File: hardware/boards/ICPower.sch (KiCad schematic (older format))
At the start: 2 parts

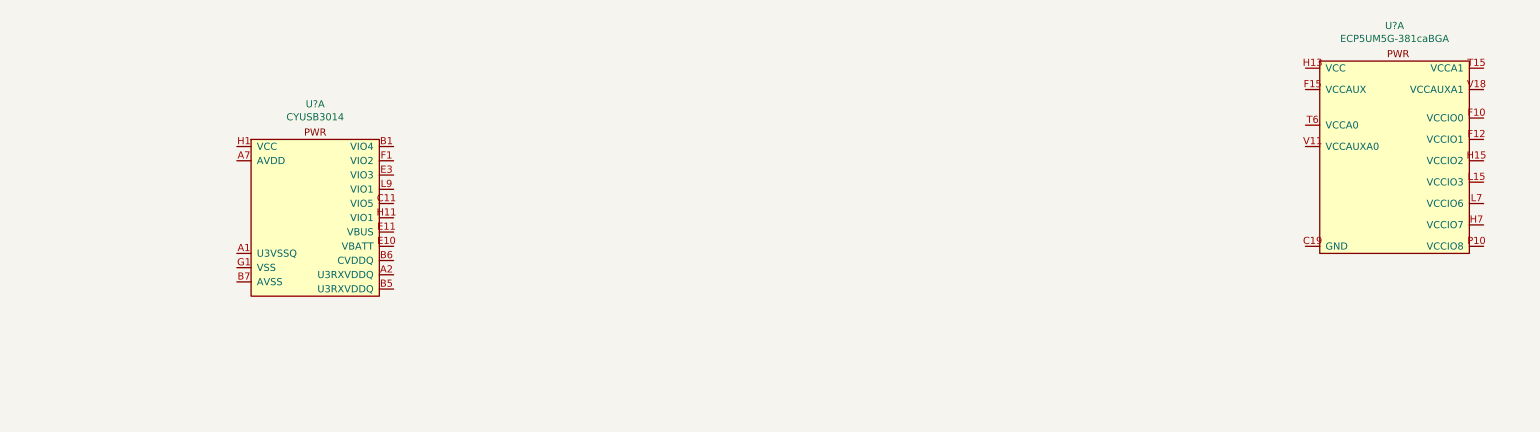
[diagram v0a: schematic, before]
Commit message: Updated part mfr and added the proper part numbers
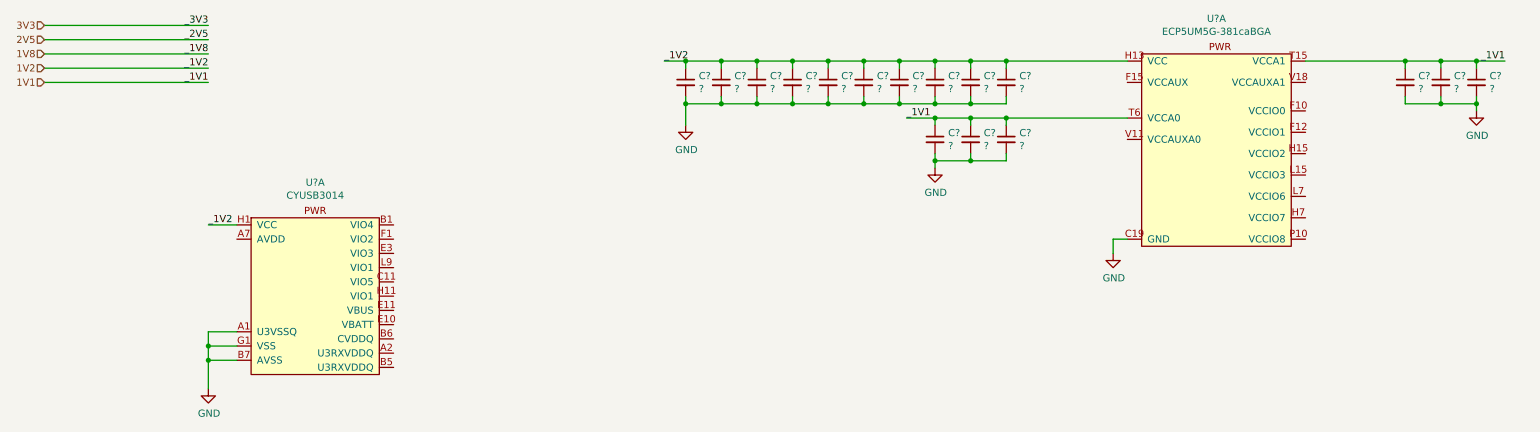
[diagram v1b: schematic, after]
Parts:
- added C? (x16): ?, symbol Device:C_Small
- U?: MFR (none) -> Lattice; MPN (none) -> LFE5UM5G-85F-8BG381I
- U?: MFR (none) -> Cypress; MPN (none) -> CYUSB3014-BZXI
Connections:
- net GND: now reaches U?.B14 (GND), U?.B7 (GND), U?.C19 (GND), U?.D4 (GND), U?.F13 (GND), U?.F14 (GND), U?.F7 (GND), U?.F8 (GND), U?.G10 (GND), U?.G11 (GND), U?.G12 (GND), U?.G13 (GND), U?.G14 (GND), U?.G15 (GND), U?.G17 (GND), U?.G4 (GND), U?.G6 (GND), U?.G7 (GND), U?.G8 (GND), U?.G9 (GND), U?.H19 (GND), U?.J10 (GND), U?.J11 (GND), U?.J12 (GND), U?.J14 (GND), U?.J2 (GND), U?.J7 (GND), U?.J9 (GND), U?.K10 (GND), U?.K11 (GND), U?.K12 (GND), U?.K14 (GND), U?.K15 (GND), U?.K6 (GND), U?.K7 (GND), U?.K9 (GND), U?.L10 (GND), U?.L11 (GND), U?.L12 (GND), U?.L9 (GND), U?.M10 (GND), U?.M11 (GND), U?.M12 (GND), U?.M14 (GND), U?.M16 (GND), U?.M2 (GND), U?.M7 (GND), U?.M9 (GND), U?.N14 (GND), U?.N15 (GND), U?.N6 (GND), U?.N7 (GND), U?.P11 (GND), U?.P12 (GND), U?.P13 (GND), U?.P14 (GND), U?.P7 (GND), U?.P8 (GND), U?.R19 (GND), U?.U10 (GND), U?.U11 (GND), U?.U12 (GND), U?.U13 (GND), U?.U14 (GND), U?.U7 (GND), U?.U8 (GND), U?.U9 (GND), U?.V12 (GND), U?.V13 (GND), U?.V14 (GND), U?.V15 (GND), U?.V16 (GND), U?.V19 (GND), U?.V20 (GND), U?.V5 (GND), U?.V6 (GND), U?.V7 (GND), U?.V8 (GND), U?.V9 (GND), U?.W12 (GND), U?.W15 (GND), U?.W16 (GND), U?.W19 (GND), U?.W6 (GND), U?.W7 (GND)
- net GND: now also U?.A1 (U3VSSQ), U?.A8 (VSS), U?.B7 (AVSS), U?.B8 (VSS), U?.B9 (VSS), U?.D8 (VSS), U?.E2 (VSS), U?.G1 (VSS), U?.G11 (VSS), U?.K3 (VSS), U?.K4 (VSS), U?.L1 (VSS), U?.L11 (VSS), U?.L2 (VSS), U?.L3 (VSS), U?.L6 (VSS), C?.2, C?.2, C?.2, C?.2, C?.2, C?.2, C?.2, C?.2, C?.2, C?.2, C?.2, C?.2, C?.2, C?.2, C?.2, C?.2
- net 1V2: now reaches U?.H10 (VCC), U?.H11 (VCC), U?.H12 (VCC), U?.H13 (VCC), U?.H8 (VCC), U?.H9 (VCC), U?.J13 (VCC), U?.J8 (VCC), U?.K13 (VCC), U?.K8 (VCC), U?.L13 (VCC), U?.L8 (VCC), U?.M13 (VCC), U?.M8 (VCC), U?.N10 (VCC), U?.N11 (VCC), U?.N12 (VCC), U?.N13 (VCC), U?.N8 (VCC), U?.N9 (VCC)
- net 1V2: now also U?.B10 (VCC), U?.C3 (VCC), U?.E9 (VCC), U?.F11 (VCC), U?.H1 (VCC), U?.J11 (VCC), U?.L5 (VCC), U?.L7 (VCC), C?.1, C?.1, C?.1, C?.1, C?.1, C?.1, C?.1, C?.1, C?.1, C?.1
- net 1V1: now reaches U?.T15 (VCCA1), U?.U15 (VCCA1)
- net 1V1: now also U?.T6 (VCCA0), U?.U6 (VCCA0), C?.1, C?.1, C?.1, C?.1, C?.1, C?.1
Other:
- moved on the sheet: U?A

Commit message: Did some annotation and fixed the FPGA bank that was accidentally labled as the cypress part
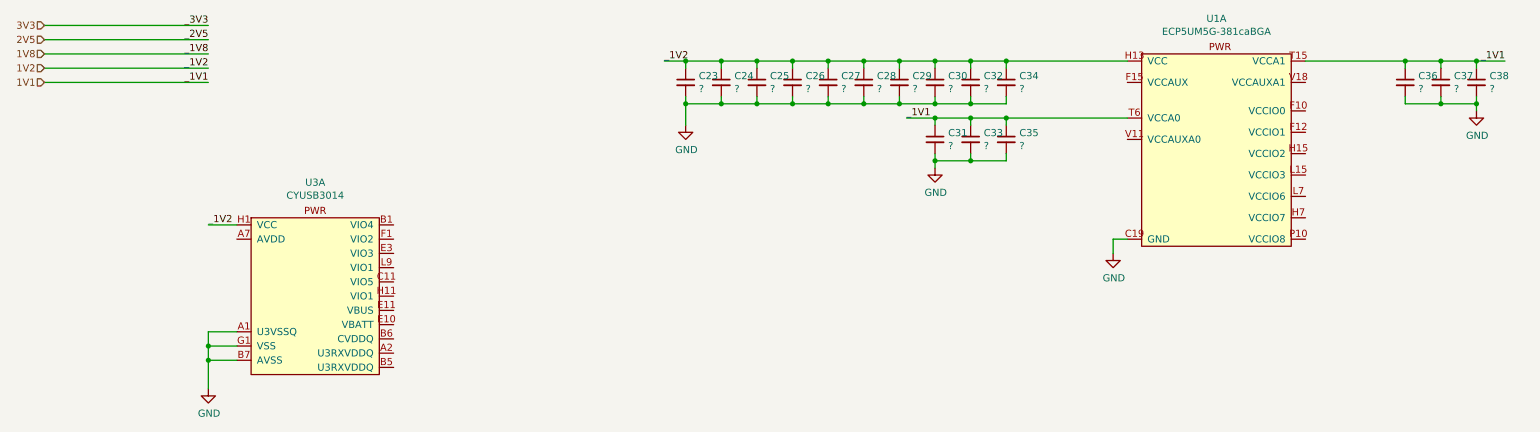
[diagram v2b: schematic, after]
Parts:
- U1: renamed from U?; footprint (none) -> lethalbit:318caBGA
- U3: renamed from U?; footprint (none) -> lethalbit:BGA-121_11x11_10.0x10.0mm
- gave numbers to parts that had none: 16
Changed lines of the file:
@@
 AR Path="/5F21FED7" Ref="U?"  Part="1"
 AR Path="/5EF66251/5F21FED7" Ref="U?"  Part="1"
-AR Path="/5EF66188/5F21FED7" Ref="U?"  Part="1"
-F 0 "U?" H 9025 1348 50  0000 C CNN
+AR Path="/5EF66188/5F21FED7" Ref="U1"  Part="1"
+F 0 "U1" H 9025 1348 50  0000 C CNN
 F 1 "ECP5UM5G-381caBGA" H 9025 1257 50  0000 C CNN
-F 2 "" H 7700 1150 50  0001 C CNN
+F 2 "lethalbit:318caBGA" H 7700 1150 50  0001 C CNN
 F 3 "" H 7700 1150 50  0001 C CNN
 F 4 "Lattice" H 9050 1000 50  0001 C CNN "MFR"
@@
 $EndComp
 $Comp
-L lethalbit:CYUSB3014 U?
+L lethalbit:CYUSB3014 U3
 U 1 1 5F31AE91
 P 2700 2600
-F 0 "U?" H 2700 3398 50  0000 C CNN
+F 0 "U3" H 2700 3398 50  0000 C CNN
 F 1 "CYUSB3014" H 2700 3307 50  0000 C CNN
-F 2 "" H 2700 3300 50  0001 C CNN
+F 2 "lethalbit:BGA-121_11x11_10.0x10.0mm" H 2700 3300 50  0001 C CNN
 F 3 "" H 2700 3300 50  0001 C CNN
 F 4 "Cypress" H 2700 2600 50  0001 C CNN "MFR"
@@
 $EndComp
 $Comp
-L power:GND #PWR?
+L power:GND #PWR0113
 U 1 1 5F6ECAA7
 P 1950 3250
-F 0 "#PWR?" H 1950 3000 50  0001 C CNN
+F 0 "#PWR0113" H 1950 3000 50  0001 C CNN
 F 1 "GND" H 1955 3077 50  0000 C CNN
 F 2 "" H 1950 3250 50  0001 C CNN
@@
 $EndComp
 $Comp
-L power:GND #PWR?
+L power:GND #PWR0114
 U 1 1 5F6F17E3
 P 8300 2300
-F 0 "#PWR?" H 8300 2050 50  0001 C CNN
+F 0 "#PWR0114" H 8300 2050 50  0001 C CNN
 F 1 "GND" H 8305 2127 50  0000 C CNN
 F 2 "" H 8300 2300 50  0001 C CNN
@@
 	1950 3050 1950 3250
 $Comp
-L Device:C_Small C?
+L Device:C_Small C30
 U 1 1 5F7003DA
 P 7050 1100
-F 0 "C?" H 7142 1146 50  0000 L CNN
+F 0 "C30" H 7142 1146 50  0000 L CNN
 F 1 "?" H 7142 1055 50  0000 L CNN
 F 2 "" H 7050 1100 50  0001 C CNN
@@
 $EndComp
 $Comp
-L Device:C_Small C?
+L Device:C_Small C29
 U 1 1 5F714758
 P 6800 1100
-F 0 "C?" H 6892 1146 50  0000 L CNN
+F 0 "C29" H 6892 1146 50  0000 L CNN
 F 1 "?" H 6892 1055 50  0000 L CNN
 F 2 "" H 6800 1100 50  0001 C CNN
@@
 $EndComp
 $Comp
-L Device:C_Small C?
+L Device:C_Small C34
 U 1 1 5F7163B0
 P 7550 1100
-F 0 "C?" H 7642 1146 50  0000 L CNN
+F 0 "C34" H 7642 1146 50  0000 L CNN
 F 1 "?" H 7642 1055 50  0000 L CNN
 F 2 "" H 7550 1100 50  0001 C CNN
@@
 $EndComp
 $Comp
-L Device:C_Small C?
+L Device:C_Small C32
 U 1 1 5F7163B8
 P 7300 1100
-F 0 "C?" H 7392 1146 50  0000 L CNN
+F 0 "C32" H 7392 1146 50  0000 L CNN
 F 1 "?" H 7392 1055 50  0000 L CNN
 F 2 "" H 7300 1100 50  0001 C CNN
@@
 $EndComp
 $Comp
-L Device:C_Small C?
+L Device:C_Small C28
 U 1 1 5F7189A8
 P 6550 1100
-F 0 "C?" H 6642 1146 50  0000 L CNN
+F 0 "C28" H 6642 1146 50  0000 L CNN
 F 1 "?" H 6642 1055 50  0000 L CNN
 F 2 "" H 6550 1100 50  0001 C CNN
@@
 $EndComp
 $Comp
-L Device:C_Small C?
+L Device:C_Small C27
 U 1 1 5F7189B0
 P 6300 1100
-F 0 "C?" H 6392 1146 50  0000 L CNN
+F 0 "C27" H 6392 1146 50  0000 L CNN
 F 1 "?" H 6392 1055 50  0000 L CNN
 F 2 "" H 6300 1100 50  0001 C CNN
@@
 $EndComp
 $Comp
-L Device:C_Small C?
+L Device:C_Small C26
 U 1 1 5F719D80
 P 6050 1100
-F 0 "C?" H 6142 1146 50  0000 L CNN
+F 0 "C26" H 6142 1146 50  0000 L CNN
 F 1 "?" H 6142 1055 50  0000 L CNN
 F 2 "" H 6050 1100 50  0001 C CNN
@@
 $EndComp
 $Comp
-L Device:C_Small C?
+L Device:C_Small C25
 U 1 1 5F719D88
 P 5800 1100
-F 0 "C?" H 5892 1146 50  0000 L CNN
+F 0 "C25" H 5892 1146 50  0000 L CNN
 F 1 "?" H 5892 1055 50  0000 L CNN
 F 2 "" H 5800 1100 50  0001 C CNN
@@
 $EndComp
 $Comp
-L Device:C_Small C?
+L Device:C_Small C24
 U 1 1 5F71A5B0
 P 5550 1100
-F 0 "C?" H 5642 1146 50  0000 L CNN
+F 0 "C24" H 5642 1146 50  0000 L CNN
 F 1 "?" H 5642 1055 50  0000 L CNN
 F 2 "" H 5550 1100 50  0001 C CNN
@@
 $EndComp
 $Comp
-L Device:C_Small C?
+L Device:C_Small C23
 U 1 1 5F71A5B8
 P 5300 1100
-F 0 "C?" H 5392 1146 50  0000 L CNN
+F 0 "C23" H 5392 1146 50  0000 L CNN
 F 1 "?" H 5392 1055 50  0000 L CNN
 F 2 "" H 5300 1100 50  0001 C CNN
@@
 $EndComp
 $Comp
-L power:GND #PWR?
+L power:GND #PWR0115
 U 1 1 5F720B5E
 P 5300 1400
-F 0 "#PWR?" H 5300 1150 50  0001 C CNN
+F 0 "#PWR0115" H 5300 1150 50  0001 C CNN
 F 1 "GND" H 5305 1227 50  0000 C CNN
 F 2 "" H 5300 1400 50  0001 C CNN
@@
 	5550 950  5800 950
 $Comp
-L Device:C_Small C?
+L Device:C_Small C31
 U 1 1 5F73F45A
 P 7050 1500
-F 0 "C?" H 7142 1546 50  0000 L CNN
+F 0 "C31" H 7142 1546 50  0000 L CNN
 F 1 "?" H 7142 1455 50  0000 L CNN
 F 2 "" H 7050 1500 50  0001 C CNN
@@
 $EndComp
 $Comp
-L Device:C_Small C?
+L Device:C_Small C35
 U 1 1 5F73F462
 P 7550 1500
-F 0 "C?" H 7642 1546 50  0000 L CNN
+F 0 "C35" H 7642 1546 50  0000 L CNN
 F 1 "?" H 7642 1455 50  0000 L CNN
 F 2 "" H 7550 1500 50  0001 C CNN
@@
 $EndComp
 $Comp
-L Device:C_Small C?
+L Device:C_Small C33
 U 1 1 5F73F46A
 P 7300 1500
-F 0 "C?" H 7392 1546 50  0000 L CNN
+F 0 "C33" H 7392 1546 50  0000 L CNN
 F 1 "?" H 7392 1455 50  0000 L CNN
 F 2 "" H 7300 1500 50  0001 C CNN
@@
 $EndComp
 $Comp
-L Device:C_Small C?
+L Device:C_Small C36
 U 1 1 5F742DBD
 P 10350 1100
-F 0 "C?" H 10442 1146 50  0000 L CNN
+F 0 "C36" H 10442 1146 50  0000 L CNN
 F 1 "?" H 10442 1055 50  0000 L CNN
 F 2 "" H 10350 1100 50  0001 C CNN
@@
 $EndComp
 $Comp
-L Device:C_Small C?
+L Device:C_Small C38
 U 1 1 5F742DC5
 P 10850 1100
-F 0 "C?" H 10942 1146 50  0000 L CNN
+F 0 "C38" H 10942 1146 50  0000 L CNN
 F 1 "?" H 10942 1055 50  0000 L CNN
 F 2 "" H 10850 1100 50  0001 C CNN
@@
 $EndComp
 $Comp
-L Device:C_Small C?
+L Device:C_Small C37
 U 1 1 5F742DCD
 P 10600 1100
-F 0 "C?" H 10692 1146 50  0000 L CNN
+F 0 "C37" H 10692 1146 50  0000 L CNN
 F 1 "?" H 10692 1055 50  0000 L CNN
 F 2 "" H 10600 1100 50  0001 C CNN
@@
 $EndComp
 $Comp
-L power:GND #PWR?
+L power:GND #PWR0116
 U 1 1 5F75CB43
 P 7050 1700
-F 0 "#PWR?" H 7050 1450 50  0001 C CNN
+F 0 "#PWR0116" H 7050 1450 50  0001 C CNN
 F 1 "GND" H 7055 1527 50  0000 C CNN
 F 2 "" H 7050 1700 50  0001 C CNN
@@
 	7550 1350 8400 1350
 $Comp
-L power:GND #PWR?
+L power:GND #PWR0117
 U 1 1 5F76BEEC
 P 10850 1300
-F 0 "#PWR?" H 10850 1050 50  0001 C CNN
+F 0 "#PWR0117" H 10850 1050 50  0001 C CNN
 F 1 "GND" H 10855 1127 50  0000 C CNN
 F 2 "" H 10850 1300 50  0001 C CNN

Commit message: Some more mist schematic edits
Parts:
- U1: DIGIKEY_PN (none) -> 220-2112-ND
- U3: DIGIKEY_PN (none) -> 428-3130-ND
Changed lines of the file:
@@
 F 4 "Lattice" H 9050 1000 50  0001 C CNN "MFR"
 F 5 "LFE5UM5G-85F-8BG381I" H 9050 1000 50  0001 C CNN "MPN"
+F 6 "220-2112-ND" H 9050 1000 50  0001 C CNN "DIGIKEY_PN"
 	1    9050 1000
 	1    0    0    -1
@@
 F 4 "Cypress" H 2700 2600 50  0001 C CNN "MFR"
 F 5 " CYUSB3014-BZXI" H 2700 2600 50  0001 C CNN "MPN"
+F 6 "428-3130-ND" H 2700 2600 50  0001 C CNN "DIGIKEY_PN"
 	1    2700 2600
 	1    0    0    -1

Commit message: Lots of small updates, getting values specified for parts, switched the BJT to NFETs
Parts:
- C23, C24, C25, C26, C27, C33, C37: value ? -> 10nF; footprint (none) -> Capacitor_SMD:C_0402_1005Metric; MFR (none) -> KEMET; MPN (none) -> C0402C103M5RACTU
- C28, C29, C30, C31, C32, C34, C36: value ? -> 100nF; footprint (none) -> Capacitor_SMD:C_0402_1005Metric; MFR (none) -> KEMET; MPN (none) -> C0402C104M8PACTU
- C35, C38: value ? -> 1nF; footprint (none) -> Capacitor_SMD:C_0402_1005Metric; MFR (none) -> KEMET; MPN (none) -> C0402C102K5RACTU
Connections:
- net 1V1 is gone; now on net 1V2: C31.1, C33.1, C35.1, C36.1, C37.1, C38.1, U1.T15 (VCCA1), U1.T6 (VCCA0), U1.U15 (VCCA1), U1.U6 (VCCA0)
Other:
- moved on the sheet: C31, C33, C38

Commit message: Some strugglebusting on getting the ERC errors cleaned up a bit
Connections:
- no-connect marks 0 -> 21
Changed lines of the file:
@@
 Wire Wire Line
 	9650 950  10150 950
+NoConn ~ 2150 2200
+NoConn ~ 3250 2100
+NoConn ~ 3250 2200
+NoConn ~ 3250 2300
+NoConn ~ 3250 2400
+NoConn ~ 3250 2500
+NoConn ~ 3250 2600
+NoConn ~ 3250 2700
+NoConn ~ 3250 2800
+NoConn ~ 3250 2900
+NoConn ~ 3250 3000
+NoConn ~ 3250 3100
+NoConn ~ 8400 1500
+NoConn ~ 8400 1100
+NoConn ~ 9650 1300
+NoConn ~ 9650 1450
+NoConn ~ 9650 1600
+NoConn ~ 9650 1750
+NoConn ~ 9650 1900
+NoConn ~ 9650 2050
+NoConn ~ 9650 2200
 $EndSCHEMATC
